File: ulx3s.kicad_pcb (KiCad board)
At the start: 4 copper layers, 94 x 50.8 mm, 113 parts, among them J1 CONN_02X20, J2 CONN_02X20, J3 WIFI_OFF, Q1 BC857, Q2 2N7002, U1 LFE5U-25F-6BG381C, U10 S25FL164K0XMFI011, U11 PCA9306DCTR, U2 ESP-32S, U3 AP3429A, U4 AP3429A, U5 AP3429A, U6 FT231XS, U7 PCF8523, U9 MT48LC16M16A2TG, Y1 FNETHE025, Y2 32768Hz

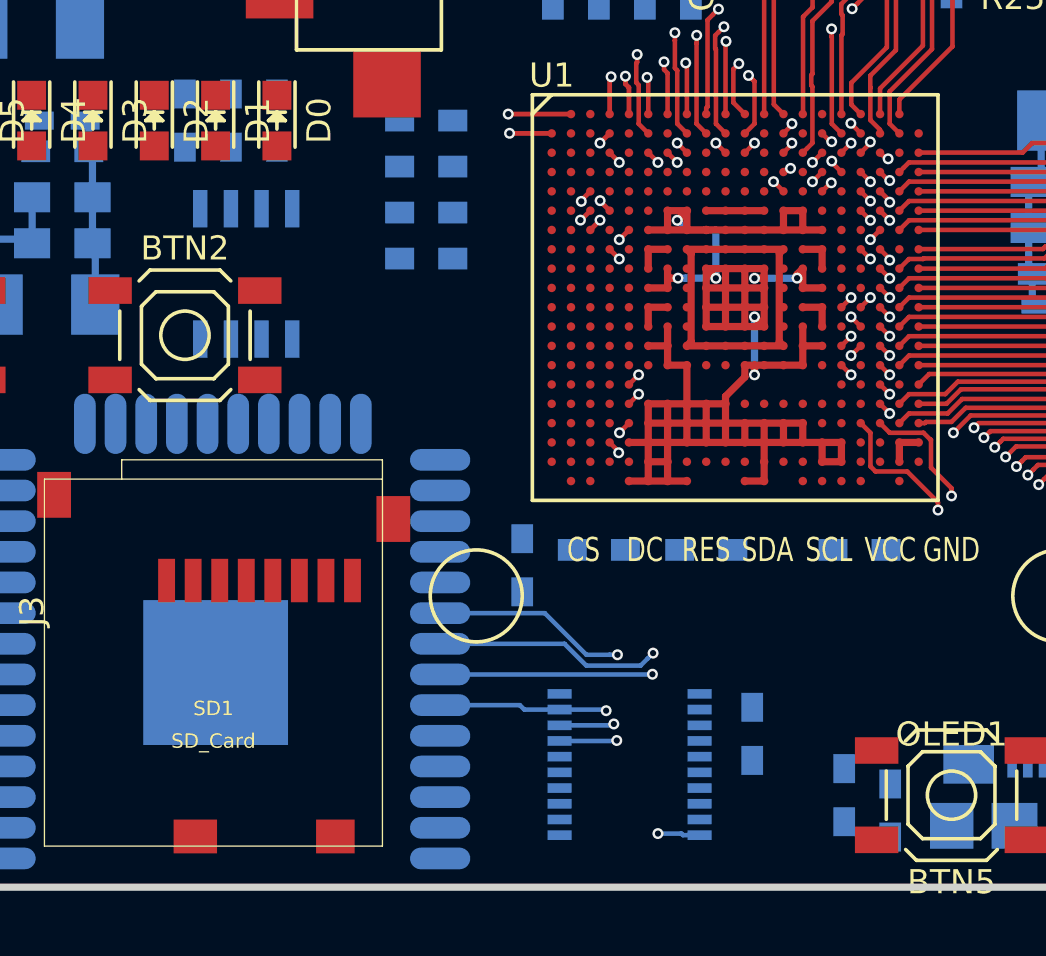
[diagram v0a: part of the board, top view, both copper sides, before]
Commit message: routing spi flash lines
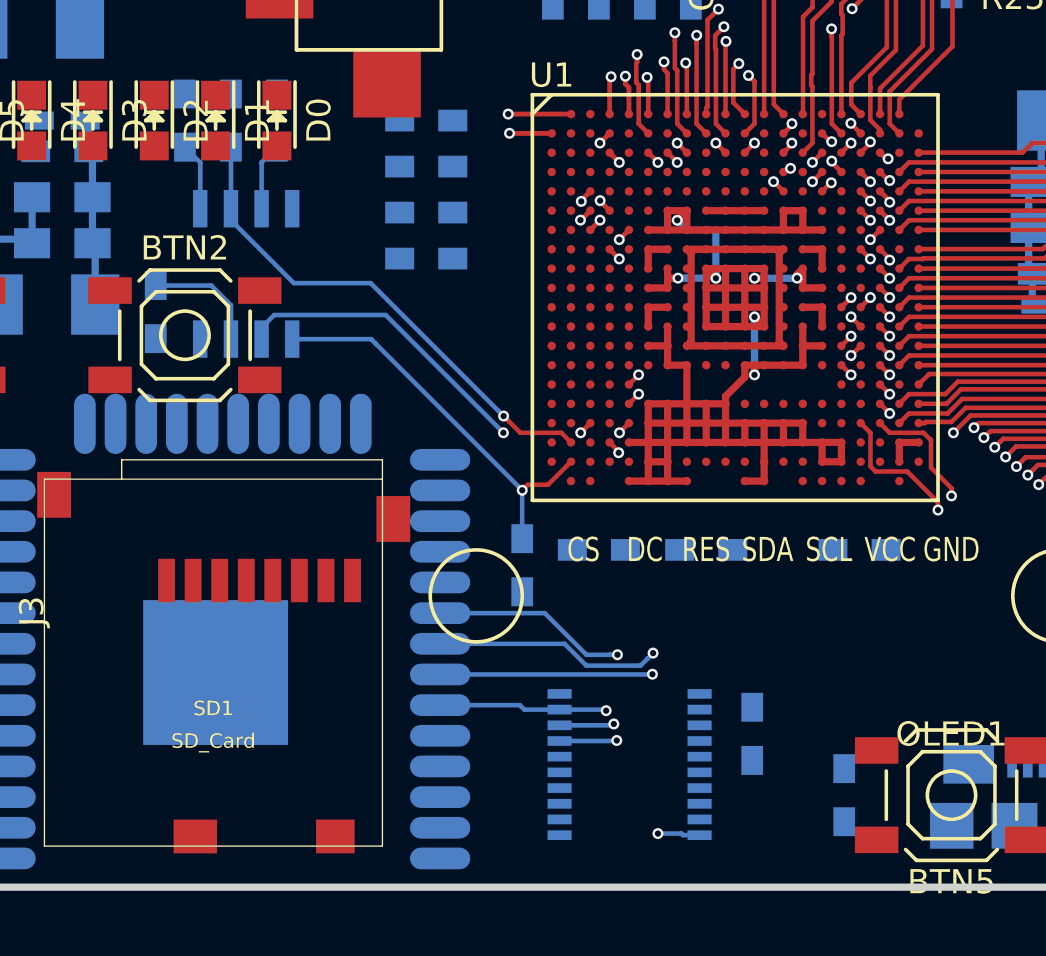
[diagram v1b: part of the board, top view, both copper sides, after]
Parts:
- moved R12 36.8 mm to (114.5, 88.4)
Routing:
- net /flash/FLASH_MISO: track 0.00 -> 20.9 mm, vias 0 -> 1
- net /flash/FLASH_MOSI: track 0.00 -> 16.6 mm, vias 0 -> 1
- net /flash/FLASH_SCK: track 0.00 -> 16.5 mm, vias 0 -> 2
- net /flash/FLASH_nHOLD: track 0.00 -> 4.86 mm
- net /flash/FLASH_nWP: track 0.00 -> 2.81 mm
- net /flash/FLASH_nCS: track 0.00 -> 2.81 mm
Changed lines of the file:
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@@
     (thickness 1.6)
     (drawings 6)
-    (tracks 1269)
+    (tracks 1304)
     (zones 0)
     (modules 113)
@@
   )
   (module Resistors_SMD:R_0603_HandSoldering (layer B.Cu)
-    (at 144.9 109.045 90)
+    (at 114.48 88.4 90)
     (descr "Resistor SMD 0603, hand soldering")
     (tags "resistor 0603")
@@
   (segment (start 144.48 92.2) (end 144.88 92.6) (width 0.19) (layer F.Cu) (net 93))
   (via (at 144.88 92.6) (size 0.454) (drill 0.254) (layers F.Cu B.Cu) (net 93))
+  (segment (start 118.865 84.12) (end 118.865 82.205) (width 0.19) (layer B.Cu) (net 94))
+  (segment (start 118.865 82.205) (end 119.5 81.57) (width 0.19) (layer B.Cu) (net 94))
+  (segment (start 116.78 87.3) (end 117.595 88.115) (width 0.19) (layer B.Cu) (net 95))
+  (segment (start 117.595 88.115) (end 117.595 89.52) (width 0.19) (layer B.Cu) (net 95))
+  (segment (start 114.48 87.3) (end 116.78 87.3) (width 0.19) (layer B.Cu) (net 95))
+  (segment (start 120.135 89.52) (end 123.4 89.52) (width 0.19) (layer B.Cu) (net 96))
+  (segment (start 123.4 89.52) (end 123.6 89.72) (width 0.19) (layer B.Cu) (net 96))
+  (segment (start 123.6 89.72) (end 129.66 95.78) (width 0.19) (layer B.Cu) (net 96))
+  (segment (start 129.66 95.78) (end 129.886999 95.553001) (width 0.19) (layer F.Cu) (net 96))
+  (segment (start 129.886999 95.553001) (end 130.726999 95.553001) (width 0.19) (layer F.Cu) (net 96))
+  (segment (start 130.726999 95.553001) (end 131.505001 94.774999) (width 0.19) (layer F.Cu) (net 96))
+  (segment (start 131.505001 94.774999) (end 131.68 94.6) (width 0.19) (layer F.Cu) (net 96))
+  (via (at 129.66 95.78) (size 0.454) (drill 0.254) (layers F.Cu B.Cu) (net 96))
+  (segment (start 129.66 95.78) (end 129.66 97.785) (width 0.19) (layer B.Cu) (net 96))
+  (segment (start 128.661809 92.481103) (end 128.888808 92.708102) (width 0.19) (layer B.Cu) (net 97))
+  (segment (start 123.380706 87.2) (end 128.661809 92.481103) (width 0.19) (layer B.Cu) (net 97))
+  (segment (start 120.2 87.2) (end 123.380706 87.2) (width 0.19) (layer B.Cu) (net 97))
+  (segment (start 117.595 84.12) (end 117.595 84.595) (width 0.19) (layer B.Cu) (net 97))
+  (segment (start 117.595 84.595) (end 120.2 87.2) (width 0.19) (layer B.Cu) (net 97))
+  (segment (start 129.115807 92.935101) (end 128.888808 92.708102) (width 0.19) (layer F.Cu) (net 97))
+  (segment (start 129.580706 93.4) (end 129.115807 92.935101) (width 0.19) (layer F.Cu) (net 97))
+  (segment (start 131.28 93.4) (end 129.580706 93.4) (width 0.19) (layer F.Cu) (net 97))
+  (segment (start 131.68 93.8) (end 131.28 93.4) (width 0.19) (layer F.Cu) (net 97))
+  (via (at 128.888808 92.708102) (size 0.454) (drill 0.254) (layers F.Cu B.Cu) (net 97))
+  (segment (start 117.595 84.12) (end 117.595 81.57) (width 0.19) (layer B.Cu) (net 97))
+  (segment (start 132.08 93.4) (end 132.48 93) (width 0.19) (layer F.Cu) (net 98))
+  (via (at 132.08 93.4) (size 0.454) (drill 0.254) (layers F.Cu B.Cu) (net 98))
+  (segment (start 128.88 93.4) (end 132.08 93.4) (width 0.19) (layer In1.Cu) (net 98))
+  (segment (start 124.002999 88.522999) (end 128.88 93.4) (width 0.19) (layer B.Cu) (net 98))
+  (via (at 128.88 93.4) (size 0.454) (drill 0.254) (layers F.Cu B.Cu) (net 98))
+  (segment (start 118.865 89.52) (end 118.865 89.045) (width 0.19) (layer B.Cu) (net 98))
+  (segment (start 118.865 89.045) (end 119.387001 88.522999) (width 0.19) (layer B.Cu) (net 98))
+  (segment (start 119.387001 88.522999) (end 124.002999 88.522999) (width 0.19) (layer B.Cu) (net 98))
+  (segment (start 116.325 84.12) (end 116.325 82.205) (width 0.19) (layer B.Cu) (net 99))
+  (segment (start 116.325 82.205) (end 115.69 81.57) (width 0.19) (layer B.Cu) (net 99))
   (segment (start 140.48 80.2) (end 140.08 79.8) (width 0.19) (layer F.Cu) (net 118))
   (segment (start 140.08 79.8) (end 140.08 74.4) (width 0.19) (layer F.Cu) (net 118))

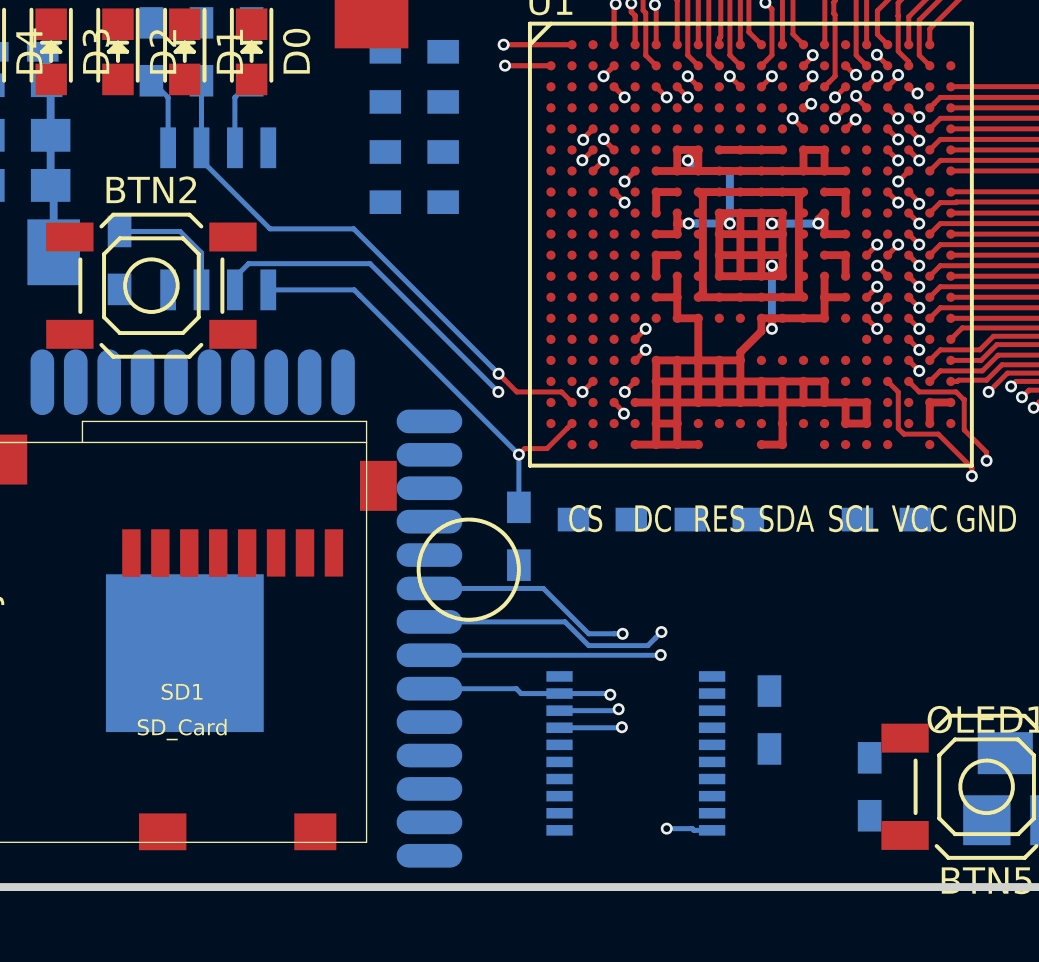
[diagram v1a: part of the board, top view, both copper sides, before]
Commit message: moving some resistor near flash chip
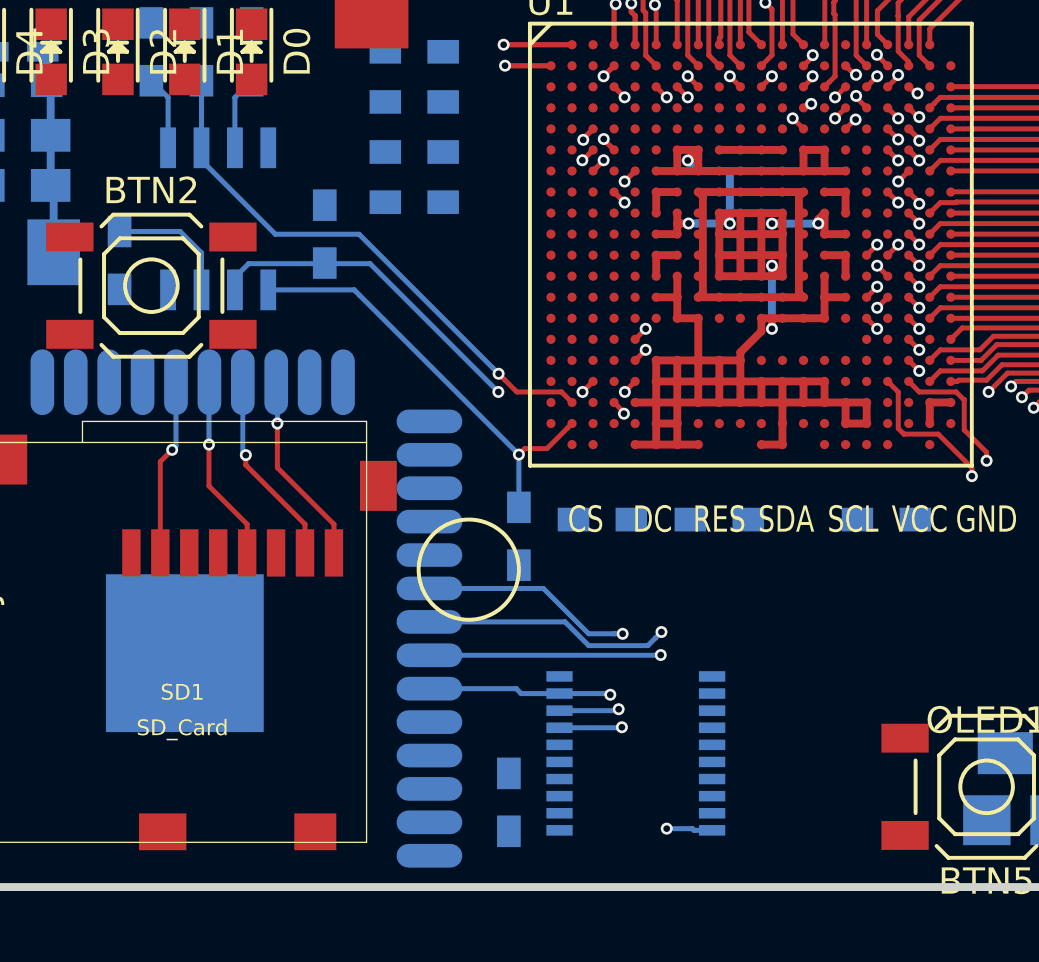
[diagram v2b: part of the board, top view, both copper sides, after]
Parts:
- moved R29 29.5 mm to (122.3, 87.4), turned to 270 degrees
- moved R9 10.4 mm to (129.3, 109.0), turned to 270 degrees
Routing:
- net SD_D0: track 0.00 -> 7.47 mm, vias 0 -> 1
- net SD_D1: track 0.00 -> 7.40 mm, vias 0 -> 1
- net SD_CLK: track 0.00 -> 7.10 mm, vias 0 -> 1
- net SD_CMD: track 0.00 -> 6.74 mm, vias 0 -> 1
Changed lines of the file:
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@@
   (general
     (links 570)
-    (no_connects 291)
+    (no_connects 279)
     (area 71.010001 43.48 197.572001 118.732339)
     (thickness 1.6)
     (drawings 6)
-    (tracks 1304)
+    (tracks 1327)
     (zones 0)
     (modules 113)
@@
   )
   (module Resistors_SMD:R_0603_HandSoldering (layer B.Cu)
-    (at 139.185 105.87 90)
+    (at 129.28 109 270)
     (descr "Resistor SMD 0603, hand soldering")
     (tags "resistor 0603")
     (attr smd)
-    (fp_text reference R9 (at 0 1.9 90) (layer B.SilkS)
+    (fp_text reference R9 (at 0 1.9 270) (layer B.SilkS)
       (effects (font (size 1 1) (thickness 0.15)) (justify mirror))
     )
-    (fp_text value 15k (at 0 -1.9 90) (layer B.Fab)
+    (fp_text value 15k (at 0 -1.9 270) (layer B.Fab)
       (effects (font (size 1 1) (thickness 0.15)) (justify mirror))
     )
@@
     (fp_line (start 0.5 -0.675) (end -0.5 -0.675) (layer B.SilkS) (width 0.15))
     (fp_line (start -0.5 0.675) (end 0.5 0.675) (layer B.SilkS) (width 0.15))
-    (pad 1 smd rect (at -1.1 0 90) (size 1.2 0.9) (layers B.Cu B.Paste B.Mask)
+    (pad 1 smd rect (at -1.1 0 270) (size 1.2 0.9) (layers B.Cu B.Paste B.Mask)
       (net 53 nRESET))
-    (pad 2 smd rect (at 1.1 0 90) (size 1.2 0.9) (layers B.Cu B.Paste B.Mask)
+    (pad 2 smd rect (at 1.1 0 270) (size 1.2 0.9) (layers B.Cu B.Paste B.Mask)
       (net 54 /usb/FT3V3))
     (model Resistors_SMD.3dshapes/R_0603_HandSoldering.wrl
@@
   )
   (module Resistors_SMD:R_0603_HandSoldering (layer B.Cu)
-    (at 142.995 108.41 90)
+    (at 122.28 87.4 270)
     (descr "Resistor SMD 0603, hand soldering")
     (tags "resistor 0603")
     (attr smd)
-    (fp_text reference R29 (at 0 1.9 90) (layer B.SilkS)
+    (fp_text reference R29 (at 0 1.9 270) (layer B.SilkS)
       (effects (font (size 1 1) (thickness 0.15)) (justify mirror))
     )
-    (fp_text value 1k (at 0 -1.9 90) (layer B.Fab)
+    (fp_text value 1k (at 0 -1.9 270) (layer B.Fab)
       (effects (font (size 1 1) (thickness 0.15)) (justify mirror))
     )
@@
     (fp_line (start 0.5 -0.675) (end -0.5 -0.675) (layer B.SilkS) (width 0.15))
     (fp_line (start -0.5 0.675) (end 0.5 0.675) (layer B.SilkS) (width 0.15))
-    (pad 1 smd rect (at -1.1 0 90) (size 1.2 0.9) (layers B.Cu B.Paste B.Mask)
+    (pad 1 smd rect (at -1.1 0 270) (size 1.2 0.9) (layers B.Cu B.Paste B.Mask)
       (net 5 +3V3))
-    (pad 2 smd rect (at 1.1 0 90) (size 1.2 0.9) (layers B.Cu B.Paste B.Mask)
+    (pad 2 smd rect (at 1.1 0 270) (size 1.2 0.9) (layers B.Cu B.Paste B.Mask)
       (net 98 /flash/FLASH_SCK))
     (model Resistors_SMD.3dshapes/R_0603_HandSoldering.wrl
@@
   (segment (start 150.615 66.67) (end 147.615 66.67) (width 0.3) (layer B.Cu) (net 44))
   (segment (start 147.615 66.67) (end 147.38 66.435) (width 0.3) (layer B.Cu) (net 44))
+  (segment (start 116.625434 93.030338) (end 116.625434 95.454566) (width 0.19) (layer B.Cu) (net 46))
+  (segment (start 116.625434 95.454566) (end 116.48 95.6) (width 0.19) (layer B.Cu) (net 46))
+  (segment (start 116.03 99.52) (end 116.03 96.05) (width 0.19) (layer F.Cu) (net 46))
+  (segment (start 116.03 96.05) (end 116.48 95.6) (width 0.19) (layer F.Cu) (net 46))
+  (via (at 116.48 95.6) (size 0.454) (drill 0.254) (layers F.Cu B.Cu) (net 46))
+  (segment (start 117.88 95.4) (end 117.88 93.045772) (width 0.19) (layer B.Cu) (net 47))
+  (segment (start 117.88 93.045772) (end 117.895434 93.030338) (width 0.19) (layer B.Cu) (net 47))
+  (segment (start 117.88 96.98) (end 117.88 95.4) (width 0.19) (layer F.Cu) (net 47))
+  (via (at 117.88 95.4) (size 0.454) (drill 0.254) (layers F.Cu B.Cu) (net 47))
+  (segment (start 119.33 99.52) (end 119.33 98.43) (width 0.19) (layer F.Cu) (net 47))
+  (segment (start 119.33 98.43) (end 117.88 96.98) (width 0.19) (layer F.Cu) (net 47))
+  (segment (start 119.165434 93.030338) (end 119.165434 95.685434) (width 0.19) (layer B.Cu) (net 48))
+  (segment (start 119.165434 95.685434) (end 119.28 95.8) (width 0.19) (layer B.Cu) (net 48))
+  (segment (start 119.28 96.18) (end 119.28 95.8) (width 0.19) (layer F.Cu) (net 48))
+  (via (at 119.28 95.8) (size 0.454) (drill 0.254) (layers F.Cu B.Cu) (net 48))
+  (segment (start 121.53 99.52) (end 121.53 98.43) (width 0.19) (layer F.Cu) (net 48))
+  (segment (start 121.53 98.43) (end 119.28 96.18) (width 0.19) (layer F.Cu) (net 48))
+  (segment (start 120.48 94.6) (end 120.48 93.074904) (width 0.19) (layer B.Cu) (net 49))
+  (segment (start 120.48 93.074904) (end 120.435434 93.030338) (width 0.19) (layer B.Cu) (net 49))
+  (segment (start 120.48 96.28) (end 120.48 94.6) (width 0.19) (layer F.Cu) (net 49))
+  (via (at 120.48 94.6) (size 0.454) (drill 0.254) (layers F.Cu B.Cu) (net 49))
+  (segment (start 122.63 99.52) (end 122.63 98.43) (width 0.19) (layer F.Cu) (net 49))
+  (segment (start 122.63 98.43) (end 120.48 96.28) (width 0.19) (layer F.Cu) (net 49))
   (segment (start 145.28 79.6) (end 147.48 77.4) (width 0.19) (layer F.Cu) (net 52))
   (segment (start 147.48 77.4) (end 147.48 70.6) (width 0.19) (layer F.Cu) (net 52))
@@
   (via (at 129.66 95.78) (size 0.454) (drill 0.254) (layers F.Cu B.Cu) (net 96))
   (segment (start 129.66 95.78) (end 129.66 97.785) (width 0.19) (layer B.Cu) (net 96))
-  (segment (start 128.661809 92.481103) (end 128.888808 92.708102) (width 0.19) (layer B.Cu) (net 97))
-  (segment (start 123.380706 87.2) (end 128.661809 92.481103) (width 0.19) (layer B.Cu) (net 97))
-  (segment (start 120.2 87.2) (end 123.380706 87.2) (width 0.19) (layer B.Cu) (net 97))
   (segment (start 117.595 84.12) (end 117.595 84.595) (width 0.19) (layer B.Cu) (net 97))
-  (segment (start 117.595 84.595) (end 120.2 87.2) (width 0.19) (layer B.Cu) (net 97))
+  (segment (start 117.595 84.595) (end 120.405209 87.405209) (width 0.19) (layer B.Cu) (net 97))
+  (segment (start 120.405209 87.405209) (end 123.585915 87.405209) (width 0.19) (layer B.Cu) (net 97))
+  (segment (start 123.585915 87.405209) (end 128.661809 92.481103) (width 0.19) (layer B.Cu) (net 97))
+  (segment (start 128.661809 92.481103) (end 128.888808 92.708102) (width 0.19) (layer B.Cu) (net 97))
   (segment (start 129.115807 92.935101) (end 128.888808 92.708102) (width 0.19) (layer F.Cu) (net 97))
   (segment (start 129.580706 93.4) (end 129.115807 92.935101) (width 0.19) (layer F.Cu) (net 97))

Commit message: reducing minimal drill size to 0.2 mm as recommended in lattice BGA guide. Seeedstudio meets this capabilities OSHpark doesn't
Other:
- net class BGA: via_dia 0.454 -> 0.4; via_drill 0.254 -> 0.2
- net class Minimal: via_dia 0.454 -> 0.4; via_drill 0.254 -> 0.2
- rule via_min_drill: 0.254 -> 0.2
- rule via_min_size: 0.454 -> 0.4
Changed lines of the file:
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@@
     (via_size 0.454)
     (via_drill 0.254)
-    (via_min_size 0.454)
-    (via_min_drill 0.254)
+    (via_min_size 0.4)
+    (via_min_drill 0.2)
     (uvia_size 0.3)
     (uvia_drill 0.1)
@@
     (clearance 0.127)
     (trace_width 0.19)
-    (via_dia 0.454)
-    (via_drill 0.254)
+    (via_dia 0.4)
+    (via_drill 0.2)
     (uvia_dia 0.3)
     (uvia_drill 0.1)
@@
     (clearance 0.127)
     (trace_width 0.127)
-    (via_dia 0.454)
-    (via_drill 0.254)
+    (via_dia 0.4)
+    (via_drill 0.2)
     (uvia_dia 0.3)
     (uvia_drill 0.1)
